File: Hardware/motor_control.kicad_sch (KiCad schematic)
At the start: 5 parts, among them J5 Conn_01x02_Male, U5 DRV8212P

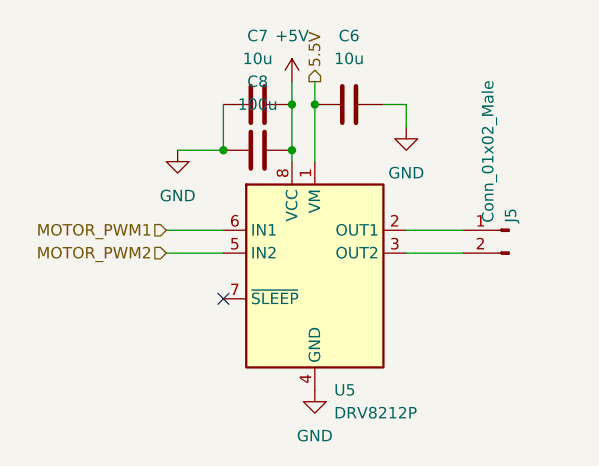
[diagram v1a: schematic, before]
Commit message: Modified power
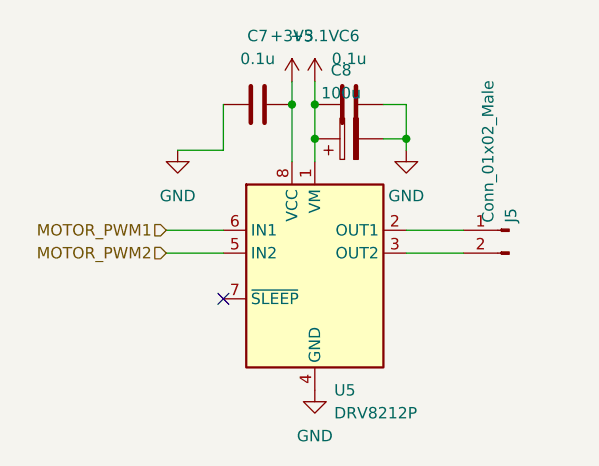
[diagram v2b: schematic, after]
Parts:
- removed C8: 100u, symbol Device:C
- added C8: 100u, symbol Device:C_Polarized
- C6, C7: value 10u -> 0.1u
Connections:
- net GND: now also C8.2
- net +5V renamed +3V3
- net 5.5V renamed +5.1V
- net +5.1V: now also C8.1
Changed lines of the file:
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@@
 	(paper "A4")
+	(junction
+		(at 180.34 54.61)
+		(diameter 0)
+		(color 0 0 0 0)
+	)
 	(junction
 		(at 177.8 50.8)
@@
 	)
 	(junction
-		(at 177.8 55.88)
+		(at 190.5 54.61)
 		(diameter 0)
 		(color 0 0 0 0)
@@
 		(color 0 0 0 0)
 	)
-	(junction
-		(at 170.18 55.88)
-		(diameter 0)
-		(color 0 0 0 0)
-	)
 	(no_connect
 		(at 170.18 72.39)
@@
 	(wire
 		(pts
-			(xy 177.8 50.8) (xy 177.8 55.88)
-		)
-		(stroke
-			(width 0)
-			(type default)
-		)
-	)
-	(wire
-		(pts
-			(xy 177.8 55.88) (xy 177.8 57.15)
+			(xy 187.96 54.61) (xy 190.5 54.61)
+		)
+		(stroke
+			(width 0)
+			(type default)
+		)
+	)
+	(wire
+		(pts
+			(xy 177.8 50.8) (xy 177.8 57.15)
 		)
 		(stroke
@@
 	(wire
 		(pts
-			(xy 180.34 50.8) (xy 180.34 57.15)
+			(xy 180.34 50.8) (xy 180.34 54.61)
 		)
 		(stroke
@@
 	(wire
 		(pts
-			(xy 190.5 50.8) (xy 190.5 53.34)
+			(xy 190.5 54.61) (xy 190.5 55.88)
+		)
+		(stroke
+			(width 0)
+			(type default)
+		)
+	)
+	(wire
+		(pts
+			(xy 190.5 50.8) (xy 190.5 54.61)
 		)
 		(stroke
@@
 		(pts
 			(xy 165.1 55.88) (xy 170.18 55.88)
+		)
+		(stroke
+			(width 0)
+			(type default)
+		)
+	)
+	(wire
+		(pts
+			(xy 180.34 54.61) (xy 180.34 57.15)
 		)
 		(stroke
@@
 		)
 	)
-	(hierarchical_label "5.5V"
-		(shape output)
-		(at 180.34 48.26 90)
-		(effects
-			(font
-				(size 1.27 1.27)
-			)
-			(justify left)
-		)
-	)
 	(symbol
 		(lib_id "Device:C")
@@
 			)
 		)
-		(property "Value" "10u"
+		(property "Value" "0.1u"
 			(at 173.99 45.72 90)
 			(effects
@@
 		)
 		(instances
-			(project "Pi-based PCB"
+			(project "Ricardo-Cappy"
 				(path "/e4035b22-64c9-4a42-9837-ade8aec3882f/4569c248-8a44-4db3-b2ae-2ad0733be142"
 					(reference "C7")
@@
 	(symbol
 		(lib_id "power:GND")
-		(at 190.5 53.34 0)
+		(at 190.5 55.88 0)
 		(unit 1)
 		(exclude_from_sim no)
@@
 		(fields_autoplaced yes)
 		(property "Reference" "#PWR022"
-			(at 190.5 59.69 0)
+			(at 190.5 62.23 0)
 			(effects
 				(font
@@
 		)
 		(property "Value" "GND"
-			(at 190.5 58.42 0)
+			(at 190.5 60.96 0)
 			(effects
 				(font
@@
 		)
 		(property "Footprint" ""
-			(at 190.5 53.34 0)
+			(at 190.5 55.88 0)
 			(effects
 				(font
@@
 		)
 		(property "Datasheet" ""
-			(at 190.5 53.34 0)
+			(at 190.5 55.88 0)
 			(effects
 				(font
@@
 		)
 		(property "Description" "Power symbol creates a global label with name \"GND\" , ground"
-			(at 190.5 53.34 0)
-			(effects
-				(font
-					(size 1.27 1.27)
-				)
-				(hide yes)
-			)
-		)
-		(pin "1"
-		)
-		(instances
-			(project "Pi-based PCB"
+			(at 190.5 55.88 0)
+			(effects
+				(font
+					(size 1.27 1.27)
+				)
+				(hide yes)
+			)
+		)
+		(pin "1"
+		)
+		(instances
+			(project "Ricardo-Cappy"
 				(path "/e4035b22-64c9-4a42-9837-ade8aec3882f/4569c248-8a44-4db3-b2ae-2ad0733be142"
 					(reference "#PWR022")
@@
 		)
 		(instances
-			(project "Pi-based PCB"
+			(project "Ricardo-Cappy"
 				(path "/e4035b22-64c9-4a42-9837-ade8aec3882f/4569c248-8a44-4db3-b2ae-2ad0733be142"
 					(reference "#PWR020")
@@
 			)
 		)
-		(property "Value" "10u"
+		(property "Value" "0.1u"
 			(at 184.15 45.72 90)
 			(effects
@@
 		)
 		(instances
-			(project "Pi-based PCB"
+			(project "Ricardo-Cappy"
 				(path "/e4035b22-64c9-4a42-9837-ade8aec3882f/4569c248-8a44-4db3-b2ae-2ad0733be142"
 					(reference "C6")
@@
 		)
 		(instances
-			(project "Pi-based PCB"
+			(project "Ricardo-Cappy"
 				(path "/e4035b22-64c9-4a42-9837-ade8aec3882f/4569c248-8a44-4db3-b2ae-2ad0733be142"
 					(reference "J5")
@@
 	)
 	(symbol
-		(lib_id "power:+5V")
+		(lib_id "power:+3V3")
 		(at 177.8 48.26 0)
 		(unit 1)
@@
 		(dnp no)
 		(fields_autoplaced yes)
-		(property "Reference" "#PWR024"
+		(property "Reference" "#PWR014"
 			(at 177.8 52.07 0)
 			(effects
@@
 			)
 		)
-		(property "Value" "+5V"
+		(property "Value" "+3V3"
 			(at 177.8 43.18 0)
 			(effects
@@
 			)
 		)
+		(property "Description" "Power symbol creates a global label with name \"+3V3\""
+			(at 177.8 48.26 0)
+			(effects
+				(font
+					(size 1.27 1.27)
+				)
+				(hide yes)
+			)
+		)
+		(pin "1"
+		)
+		(instances
+			(project "Ricardo-Cappy"
+				(path "/e4035b22-64c9-4a42-9837-ade8aec3882f/4569c248-8a44-4db3-b2ae-2ad0733be142"
+					(reference "#PWR014")
+					(unit 1)
+				)
+			)
+		)
+	)
+	(symbol
+		(lib_id "power:+5V")
+		(at 180.34 48.26 0)
+		(unit 1)
+		(exclude_from_sim no)
+		(in_bom yes)
+		(on_board yes)
+		(dnp no)
+		(fields_autoplaced yes)
+		(property "Reference" "#PWR023"
+			(at 180.34 52.07 0)
+			(effects
+				(font
+					(size 1.27 1.27)
+				)
+				(hide yes)
+			)
+		)
+		(property "Value" "+5.1V"
+			(at 180.34 43.18 0)
+			(effects
+				(font
+					(size 1.27 1.27)
+				)
+			)
+		)
+		(property "Footprint" ""
+			(at 180.34 48.26 0)
+			(effects
+				(font
+					(size 1.27 1.27)
+				)
+				(hide yes)
+			)
+		)
+		(property "Datasheet" ""
+			(at 180.34 48.26 0)
+			(effects
+				(font
+					(size 1.27 1.27)
+				)
+				(hide yes)
+			)
+		)
 		(property "Description" "Power symbol creates a global label with name \"+5V\""
-			(at 177.8 48.26 0)
-			(effects
-				(font
-					(size 1.27 1.27)
-				)
-				(hide yes)
-			)
-		)
-		(pin "1"
-		)
-		(instances
-			(project "Pi-based PCB"
-				(path "/e4035b22-64c9-4a42-9837-ade8aec3882f/4569c248-8a44-4db3-b2ae-2ad0733be142"
-					(reference "#PWR024")
+			(at 180.34 48.26 0)
+			(effects
+				(font
+					(size 1.27 1.27)
+				)
+				(hide yes)
+			)
+		)
+		(pin "1"
+		)
+		(instances
+			(project "Ricardo-Cappy"
+				(path "/e4035b22-64c9-4a42-9837-ade8aec3882f/4569c248-8a44-4db3-b2ae-2ad0733be142"
+					(reference "#PWR023")
 					(unit 1)
 				)
@@
 		)
 		(instances
-			(project "Pi-based PCB"
+			(project "Ricardo-Cappy"
 				(path "/e4035b22-64c9-4a42-9837-ade8aec3882f/4569c248-8a44-4db3-b2ae-2ad0733be142"
 					(reference "#PWR021")
@@
 	)
 	(symbol
-		(lib_id "Device:C")
-		(at 173.99 55.88 90)
+		(lib_id "Device:C_Polarized")
+		(at 184.15 54.61 90)
 		(unit 1)
 		(exclude_from_sim no)
@@
 		(fields_autoplaced yes)
 		(property "Reference" "C8"
-			(at 173.99 48.26 90)
+			(at 183.261 46.99 90)
 			(effects
 				(font
@@
 		)
 		(property "Value" "100u"
-			(at 173.99 50.8 90)
+			(at 183.261 49.53 90)
 			(effects
 				(font
@@
 		)
 		(property "Footprint" ""
-			(at 177.8 54.9148 0)
+			(at 187.96 53.6448 0)
 			(effects
 				(font
@@
 		)
 		(property "Datasheet" "~"
-			(at 173.99 55.88 0)
-			(effects
-				(font
-					(size 1.27 1.27)
-				)
-				(hide yes)
-			)
-		)
-		(property "Description" "Unpolarized capacitor"
-			(at 173.99 55.88 0)
+			(at 184.15 54.61 0)
+			(effects
+				(font
+					(size 1.27 1.27)
+				)
+				(hide yes)
+			)
+		)
+		(property "Description" "Polarized capacitor"
+			(at 184.15 54.61 0)
 			(effects
 				(font
@@
 		)
 		(instances
-			(project "Pi-based PCB"
+			(project "Ricardo-Cappy"
 				(path "/e4035b22-64c9-4a42-9837-ade8aec3882f/4569c248-8a44-4db3-b2ae-2ad0733be142"
 					(reference "C8")
@@
 		)
 		(instances
-			(project "Pi-based PCB"
+			(project "Ricardo-Cappy"
 				(path "/e4035b22-64c9-4a42-9837-ade8aec3882f/4569c248-8a44-4db3-b2ae-2ad0733be142"
 					(reference "U5")

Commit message: Fixed power
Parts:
- removed J5: Conn_01x02_Male, TerminalBlock_Phoenix:TerminalBlock_Phoenix_PT-1,5-2-3.5-H_1x02_P3.50mm_Horizontal, symbol Connector:Conn_01x02_Male
- added TC1: Motor Out, Connector_Molex:Molex_Nano-Fit_105313-xx02_1x02_P2.50mm_Horizontal, symbol Device:Thermocouple
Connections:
- net at U5.2 (OUT1): now also TC1.2 (-)
- net at U5.3 (OUT2): now also TC1.1 (+)
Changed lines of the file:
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@@
 	(wire
 		(pts
-			(xy 190.5 64.77) (xy 196.85 64.77)
+			(xy 200.66 64.77) (xy 200.66 63.5)
+		)
+		(stroke
+			(width 0)
+			(type default)
+		)
+	)
+	(wire
+		(pts
+			(xy 190.5 64.77) (xy 200.66 64.77)
 		)
 		(stroke
@@
 	(wire
 		(pts
+			(xy 200.66 67.31) (xy 200.66 68.58)
+		)
+		(stroke
+			(width 0)
+			(type default)
+		)
+	)
+	(wire
+		(pts
 			(xy 163.83 64.77) (xy 170.18 64.77)
 		)
@@
 	(wire
 		(pts
-			(xy 190.5 67.31) (xy 196.85 67.31)
+			(xy 190.5 67.31) (xy 200.66 67.31)
 		)
 		(stroke
@@
 			)
 			(justify right)
+		)
+	)
+	(symbol
+		(lib_id "Device:Thermocouple")
+		(at 203.2 66.04 180)
+		(unit 1)
+		(exclude_from_sim no)
+		(in_bom yes)
+		(on_board yes)
+		(dnp no)
+		(property "Reference" "TC1"
+			(at 203.8858 74.295 0)
+			(effects
+				(font
+					(size 1.27 1.27)
+				)
+			)
+		)
+		(property "Value" "Motor Out"
+			(at 203.8858 71.9836 0)
+			(effects
+				(font
+					(size 1.27 1.27)
+				)
+			)
+		)
+		(property "Footprint" "Connector_Molex:Molex_Nano-Fit_105313-xx02_1x02_P2.50mm_Horizontal"
+			(at 217.805 67.31 0)
+			(effects
+				(font
+					(size 1.27 1.27)
+				)
+				(hide yes)
+			)
+		)
+		(property "Datasheet" "~"
+			(at 217.805 67.31 0)
+			(effects
+				(font
+					(size 1.27 1.27)
+				)
+				(hide yes)
+			)
+		)
+		(property "Description" ""
+			(at 203.2 66.04 0)
+			(effects
+				(font
+					(size 1.27 1.27)
+				)
+				(hide yes)
+			)
+		)
+		(pin "1"
+		)
+		(pin "2"
+		)
+		(instances
+			(project "Ricardo-Cappy"
+				(path "/e4035b22-64c9-4a42-9837-ade8aec3882f/4569c248-8a44-4db3-b2ae-2ad0733be142"
+					(reference "TC1")
+					(unit 1)
+				)
+			)
 		)
 	)
@@
 					(unit 1)
 				)
-			)
-		)
-	)
-	(symbol
-		(lib_id "Connector:Conn_01x02_Male")
-		(at 201.93 64.77 0)
-		(mirror y)
-		(unit 1)
-		(exclude_from_sim no)
-		(in_bom yes)
-		(on_board yes)
-		(dnp no)
-		(property "Reference" "J5"
-			(at 202.1297 63.9318 90)
-			(effects
-				(font
-					(size 1.27 1.27)
-				)
-				(justify left)
-			)
-		)
-		(property "Value" "Conn_01x02_Male"
-			(at 199.5928 63.9318 90)
-			(effects
-				(font
-					(size 1.27 1.27)
-				)
-				(justify left)
-			)
-		)
-		(property "Footprint" "TerminalBlock_Phoenix:TerminalBlock_Phoenix_PT-1,5-2-3.5-H_1x02_P3.50mm_Horizontal"
-			(at 201.93 64.77 0)
-			(effects
-				(font
-					(size 1.27 1.27)
-				)
-				(hide yes)
-			)
-		)
-		(property "Datasheet" "~"
-			(at 201.93 64.77 0)
-			(effects
-				(font
-					(size 1.27 1.27)
-				)
-				(hide yes)
-			)
-		)
-		(property "Description" ""
-			(at 201.93 64.77 0)
-			(effects
-				(font
-					(size 1.27 1.27)
-				)
-				(hide yes)
-			)
-		)
-		(pin "1"
-		)
-		(pin "2"
-		)
-		(instances
-			(project "Ricardo-Cappy"
-				(path "/e4035b22-64c9-4a42-9837-ade8aec3882f/4569c248-8a44-4db3-b2ae-2ad0733be142"
-					(reference "J5")
-					(unit 1)
-				)
